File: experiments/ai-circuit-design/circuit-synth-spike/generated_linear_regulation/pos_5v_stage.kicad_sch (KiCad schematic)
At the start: 9 parts

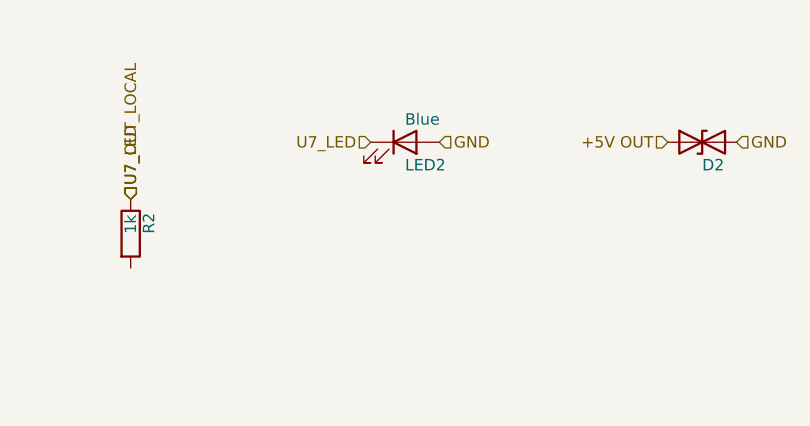
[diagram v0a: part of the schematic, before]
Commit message: fix(experiments): address deep-review findings (SPICE model, LED polarity, skill perms)
Codex review (P2) fixes on the A–D trial artifacts:
- SPICE value-sizing deck: the loop-closed check pinned FB to Vref via an ideal
  source, which floated VOUT (KCL forced VOUT==FB≈1.23V). Replaced with a
  high-gain error-amp behavioral source driving the real divider, so .op now
  genuinely solves VOUT=Vref*(1+Rtop/Rbot). Same fix in the sweep deck; FINDINGS
  method note updated.
- circuit-synth spike: Device:LED pin1=cathode/pin2=anode, but the helper wired
  the positive rail to pin1 → reverse-biased +12V/+5V indicator LEDs. Added a
  rail-aware `negative` flag; positive stages now anode→rail, negative stage
  anode→GND. Regenerated the .kicad_sch/.net/.json output to match.
- pd-schematic-review skill: added `Bash(mkdir -p __inbox*)` to allowed-tools so
  the netlist-export step doesn't block on a fresh clone (__inbox is gitignored).

Co-Authored-By: Claude Opus 4.8 (1M context) <noreply@anthropic.com>
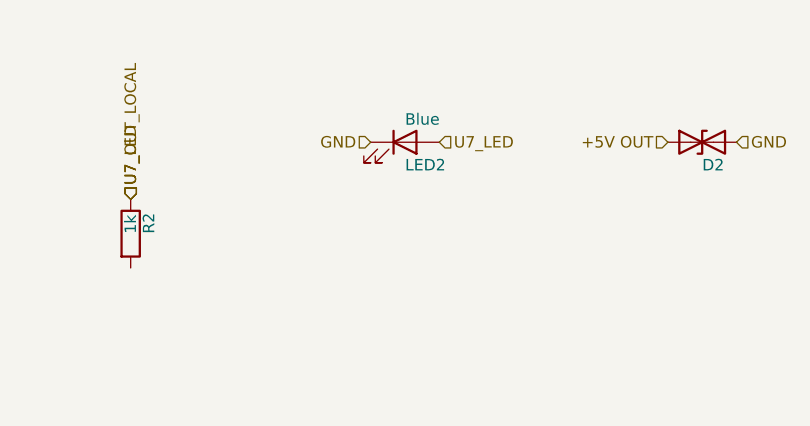
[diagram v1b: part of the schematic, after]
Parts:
- C5, C6, C7, C8, D2, F2, LED2, R2, U7: hierarchy_path /dee5fd78-2d54-41fe-ba07-6c5be7c122e4/f744ef92-40bb-442d-98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 -> /fde22f73-ec7e-4a79-83c1-d101e011a27c/6c8fbec5-5ec1-4eba-ab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; root_uuid dee5fd78-2d54-41fe-ba07-6c5be7c122e4 -> fde22f73-ec7e-4a79-83c1-d101e011a27c
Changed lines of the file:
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@@
 			)
 		)
-		(property "hierarchy_path" "/dee5fd78-2d54-41fe-ba07-6c5be7c122e4/f744ef92-40bb-442d-9874-46d0a9d8fa6f"
+		(property "hierarchy_path" "/fde22f73-ec7e-4a79-83c1-d101e011a27c/6c8fbec5-5ec1-4eba-ab3d-0a31d99ff1f6"
 			(at 40.64 35.5599 0)
 			(effects
@@
 			)
 		)
-		(property "root_uuid" "dee5fd78-2d54-41fe-ba07-6c5be7c122e4"
+		(property "root_uuid" "fde22f73-ec7e-4a79-83c1-d101e011a27c"
 			(at 40.64 35.5599 0)
 			(effects
@@
 		(instances
 			(project ""
-				(path "/dee5fd78-2d54-41fe-ba07-6c5be7c122e4/f744ef92-40bb-442d-9874-46d0a9d8fa6f"
+				(path "/fde22f73-ec7e-4a79-83c1-d101e011a27c/6c8fbec5-5ec1-4eba-ab3d-0a31d99ff1f6"
 					(reference "U7")
 					(unit 1)
@@
 			)
 		)
-		(property "hierarchy_path" "/dee5fd78-2d54-41fe-ba07-6c5be7c122e4/f744ef92-40bb-442d-9874-46d0a9d8fa6f"
+		(property "hierarchy_path" "/fde22f73-ec7e-4a79-83c1-d101e011a27c/6c8fbec5-5ec1-4eba-ab3d-0a31d99ff1f6"
 			(at 187.96 38.0999 0)
 			(effects
@@
 			)
 		)
-		(property "root_uuid" "dee5fd78-2d54-41fe-ba07-6c5be7c122e4"
+		(property "root_uuid" "fde22f73-ec7e-4a79-83c1-d101e011a27c"
 			(at 187.96 38.0999 0)
 			(effects
@@
 		(instances
 			(project ""
-				(path "/dee5fd78-2d54-41fe-ba07-6c5be7c122e4/f744ef92-40bb-442d-9874-46d0a9d8fa6f"
+				(path "/fde22f73-ec7e-4a79-83c1-d101e011a27c/6c8fbec5-5ec1-4eba-ab3d-0a31d99ff1f6"
 					(reference "C5")
 					(unit 1)
@@
 			)
 		)
-		(property "hierarchy_path" "/dee5fd78-2d54-41fe-ba07-6c5be7c122e4/f744ef92-40bb-442d-9874-46d0a9d8fa6f"
+		(property "hierarchy_path" "/fde22f73-ec7e-4a79-83c1-d101e011a27c/6c8fbec5-5ec1-4eba-ab3d-0a31d99ff1f6"
 			(at 213.36 38.0999 0)
 			(effects
@@
 			)
 		)
-		(property "root_uuid" "dee5fd78-2d54-41fe-ba07-6c5be7c122e4"
+		(property "root_uuid" "fde22f73-ec7e-4a79-83c1-d101e011a27c"
 			(at 213.36 38.0999 0)
 			(effects
@@
 		(instances
 			(project ""
-				(path "/dee5fd78-2d54-41fe-ba07-6c5be7c122e4/f744ef92-40bb-442d-9874-46d0a9d8fa6f"
+				(path "/fde22f73-ec7e-4a79-83c1-d101e011a27c/6c8fbec5-5ec1-4eba-ab3d-0a31d99ff1f6"
 					(reference "C6")
 					(unit 1)
@@
 			)
 		)
-		(property "hierarchy_path" "/dee5fd78-2d54-41fe-ba07-6c5be7c122e4/f744ef92-40bb-442d-9874-46d0a9d8fa6f"
+		(property "hierarchy_path" "/fde22f73-ec7e-4a79-83c1-d101e011a27c/6c8fbec5-5ec1-4eba-ab3d-0a31d99ff1f6"
 			(at 238.76 38.0999 0)
 			(effects
@@
 			)
 		)
-		(property "root_uuid" "dee5fd78-2d54-41fe-ba07-6c5be7c122e4"
+		(property "root_uuid" "fde22f73-ec7e-4a79-83c1-d101e011a27c"
 			(at 238.76 38.0999 0)
 			(effects
@@
 		(instances
 			(project ""
-				(path "/dee5fd78-2d54-41fe-ba07-6c5be7c122e4/f744ef92-40bb-442d-9874-46d0a9d8fa6f"
+				(path "/fde22f73-ec7e-4a79-83c1-d101e011a27c/6c8fbec5-5ec1-4eba-ab3d-0a31d99ff1f6"
 					(reference "C7")
 					(unit 1)
@@
 			)
 		)
-		(property "hierarchy_path" "/dee5fd78-2d54-41fe-ba07-6c5be7c122e4/f744ef92-40bb-442d-9874-46d0a9d8fa6f"
+		(property "hierarchy_path" "/fde22f73-ec7e-4a79-83c1-d101e011a27c/6c8fbec5-5ec1-4eba-ab3d-0a31d99ff1f6"
 			(at 264.16 38.0999 0)
 			(effects
@@
 			)
 		)
-		(property "root_uuid" "dee5fd78-2d54-41fe-ba07-6c5be7c122e4"
+		(property "root_uuid" "fde22f73-ec7e-4a79-83c1-d101e011a27c"
 			(at 264.16 38.0999 0)
 			(effects
@@
 		(instances
 			(project ""
-				(path "/dee5fd78-2d54-41fe-ba07-6c5be7c122e4/f744ef92-40bb-442d-9874-46d0a9d8fa6f"
+				(path "/fde22f73-ec7e-4a79-83c1-d101e011a27c/6c8fbec5-5ec1-4eba-ab3d-0a31d99ff1f6"
 					(reference "C8")
 					(unit 1)
@@
 			)
 		)
-		(property "hierarchy_path" "/dee5fd78-2d54-41fe-ba07-6c5be7c122e4/f744ef92-40bb-442d-9874-46d0a9d8fa6f"
+		(property "hierarchy_path" "/fde22f73-ec7e-4a79-83c1-d101e011a27c/6c8fbec5-5ec1-4eba-ab3d-0a31d99ff1f6"
 			(at 73.66 40.6399 0)
 			(effects
@@
 			)
 		)
-		(property "root_uuid" "dee5fd78-2d54-41fe-ba07-6c5be7c122e4"
+		(property "root_uuid" "fde22f73-ec7e-4a79-83c1-d101e011a27c"
 			(at 73.66 40.6399 0)
 			(effects
@@
 		(instances
 			(project ""
-				(path "/dee5fd78-2d54-41fe-ba07-6c5be7c122e4/f744ef92-40bb-442d-9874-46d0a9d8fa6f"
+				(path "/fde22f73-ec7e-4a79-83c1-d101e011a27c/6c8fbec5-5ec1-4eba-ab3d-0a31d99ff1f6"
 					(reference "F2")
 					(unit 1)
@@
 			)
 		)
-		(property "hierarchy_path" "/dee5fd78-2d54-41fe-ba07-6c5be7c122e4/f744ef92-40bb-442d-9874-46d0a9d8fa6f"
+		(property "hierarchy_path" "/fde22f73-ec7e-4a79-83c1-d101e011a27c/6c8fbec5-5ec1-4eba-ab3d-0a31d99ff1f6"
 			(at 160.02 30.4799 0)
 			(effects
@@
 			)
 		)
-		(property "root_uuid" "dee5fd78-2d54-41fe-ba07-6c5be7c122e4"
+		(property "root_uuid" "fde22f73-ec7e-4a79-83c1-d101e011a27c"
 			(at 160.02 30.4799 0)
 			(effects
@@
 		(instances
 			(project ""
-				(path "/dee5fd78-2d54-41fe-ba07-6c5be7c122e4/f744ef92-40bb-442d-9874-46d0a9d8fa6f"
+				(path "/fde22f73-ec7e-4a79-83c1-d101e011a27c/6c8fbec5-5ec1-4eba-ab3d-0a31d99ff1f6"
 					(reference "D2")
 					(unit 1)
@@
 			)
 		)
-		(property "hierarchy_path" "/dee5fd78-2d54-41fe-ba07-6c5be7c122e4/f744ef92-40bb-442d-9874-46d0a9d8fa6f"
+		(property "hierarchy_path" "/fde22f73-ec7e-4a79-83c1-d101e011a27c/6c8fbec5-5ec1-4eba-ab3d-0a31d99ff1f6"
 			(at 96.52 40.6399 0)
 			(effects
@@
 			)
 		)
-		(property "root_uuid" "dee5fd78-2d54-41fe-ba07-6c5be7c122e4"
+		(property "root_uuid" "fde22f73-ec7e-4a79-83c1-d101e011a27c"
 			(at 96.52 40.6399 0)
 			(effects
@@
 		(instances
 			(project ""
-				(path "/dee5fd78-2d54-41fe-ba07-6c5be7c122e4/f744ef92-40bb-442d-9874-46d0a9d8fa6f"
+				(path "/fde22f73-ec7e-4a79-83c1-d101e011a27c/6c8fbec5-5ec1-4eba-ab3d-0a31d99ff1f6"
 					(reference "R2")
 					(unit 1)
@@
 			)
 		)
-		(property "hierarchy_path" "/dee5fd78-2d54-41fe-ba07-6c5be7c122e4/f744ef92-40bb-442d-9874-46d0a9d8fa6f"
+		(property "hierarchy_path" "/fde22f73-ec7e-4a79-83c1-d101e011a27c/6c8fbec5-5ec1-4eba-ab3d-0a31d99ff1f6"
 			(at 127 30.4799 0)
 			(effects
@@
 			)
 		)
-		(property "root_uuid" "dee5fd78-2d54-41fe-ba07-6c5be7c122e4"
+		(property "root_uuid" "fde22f73-ec7e-4a79-83c1-d101e011a27c"
 			(at 127 30.4799 0)
 			(effects
@@
 		(instances
 			(project ""
-				(path "/dee5fd78-2d54-41fe-ba07-6c5be7c122e4/f744ef92-40bb-442d-9874-46d0a9d8fa6f"
+				(path "/fde22f73-ec7e-4a79-83c1-d101e011a27c/6c8fbec5-5ec1-4eba-ab3d-0a31d99ff1f6"
 					(reference "LED2")
 					(unit 1)
@@
 	(hierarchical_label "GND"
 		(shape input)
+		(at 120.65 25.4 180)
+		(effects
+			(font
+				(size 1.27 1.27)
+			)
+			(justify right)
+		)
+	)
+	(hierarchical_label "U7_OUT_LOCAL"
+		(shape input)
+		(at 45.72 30.48 0.0000)
+		(effects
+			(font
+				(size 1.27 1.27)
+			)
+			(justify left)
+		)
+	)
+	(hierarchical_label "U7_OUT_LOCAL"
+		(shape input)
+		(at 45.72 30.48 0.0000)
+		(effects
+			(font
+				(size 1.27 1.27)
+			)
+			(justify left)
+		)
+	)
+	(hierarchical_label "U7_OUT_LOCAL"
+		(shape input)
+		(at 236.22 29.21 90)
+		(effects
+			(font
+				(size 1.27 1.27)
+			)
+			(justify left)
+		)
+	)
+	(hierarchical_label "U7_OUT_LOCAL"
+		(shape input)
+		(at 261.62 29.21 90)
+		(effects
+			(font
+				(size 1.27 1.27)
+			)
+			(justify left)
+		)
+	)
+	(hierarchical_label "U7_OUT_LOCAL"
+		(shape input)
+		(at 71.12 31.75 90)
+		(effects
+			(font
+				(size 1.27 1.27)
+			)
+			(justify left)
+		)
+	)
+	(hierarchical_label "U7_OUT_LOCAL"
+		(shape input)
+		(at 93.98 31.75 90)
+		(effects
+			(font
+				(size 1.27 1.27)
+			)
+			(justify left)
+		)
+	)
+	(hierarchical_label "+5V OUT"
+		(shape input)
+		(at 71.12 31.75 90)
+		(effects
+			(font
+				(size 1.27 1.27)
+			)
+			(justify left)
+		)
+	)
+	(hierarchical_label "+5V OUT"
+		(shape input)
+		(at 153.67 25.4 180)
+		(effects
+			(font
+				(size 1.27 1.27)
+			)
+			(justify right)
+		)
+	)
+	(hierarchical_label "U7_LED"
+		(shape input)
+		(at 93.98 31.75 90)
+		(effects
+			(font
+				(size 1.27 1.27)
+			)
+			(justify left)
+		)
+	)
+	(hierarchical_label "U7_LED"
+		(shape input)
 		(at 128.27 25.4 0.0000)
 		(effects
@@
 		)
 	)
-	(hierarchical_label "U7_OUT_LOCAL"
-		(shape input)
-		(at 45.72 30.48 0.0000)
-		(effects
-			(font
-				(size 1.27 1.27)
-			)
-			(justify left)
-		)
-	)
-	(hierarchical_label "U7_OUT_LOCAL"
-		(shape input)
-		(at 45.72 30.48 0.0000)
-		(effects
-			(font
-				(size 1.27 1.27)
-			)
-			(justify left)
-		)
-	)
-	(hierarchical_label "U7_OUT_LOCAL"
-		(shape input)
-		(at 236.22 29.21 90)
-		(effects
-			(font
-				(size 1.27 1.27)
-			)
-			(justify left)
-		)
-	)
-	(hierarchical_label "U7_OUT_LOCAL"
-		(shape input)
-		(at 261.62 29.21 90)
-		(effects
-			(font
-				(size 1.27 1.27)
-			)
-			(justify left)
-		)
-	)
-	(hierarchical_label "U7_OUT_LOCAL"
-		(shape input)
-		(at 71.12 31.75 90)
-		(effects
-			(font
-				(size 1.27 1.27)
-			)
-			(justify left)
-		)
-	)
-	(hierarchical_label "U7_OUT_LOCAL"
-		(shape input)
-		(at 93.98 31.75 90)
-		(effects
-			(font
-				(size 1.27 1.27)
-			)
-			(justify left)
-		)
-	)
-	(hierarchical_label "+5V OUT"
-		(shape input)
-		(at 71.12 31.75 90)
-		(effects
-			(font
-				(size 1.27 1.27)
-			)
-			(justify left)
-		)
-	)
-	(hierarchical_label "+5V OUT"
-		(shape input)
-		(at 153.67 25.4 180)
-		(effects
-			(font
-				(size 1.27 1.27)
-			)
-			(justify right)
-		)
-	)
-	(hierarchical_label "U7_LED"
-		(shape input)
-		(at 93.98 31.75 90)
-		(effects
-			(font
-				(size 1.27 1.27)
-			)
-			(justify left)
-		)
-	)
-	(hierarchical_label "U7_LED"
-		(shape input)
-		(at 120.65 25.4 180)
-		(effects
-			(font
-				(size 1.27 1.27)
-			)
-			(justify right)
-		)
-	)
